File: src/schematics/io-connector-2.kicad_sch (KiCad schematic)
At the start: 1 part

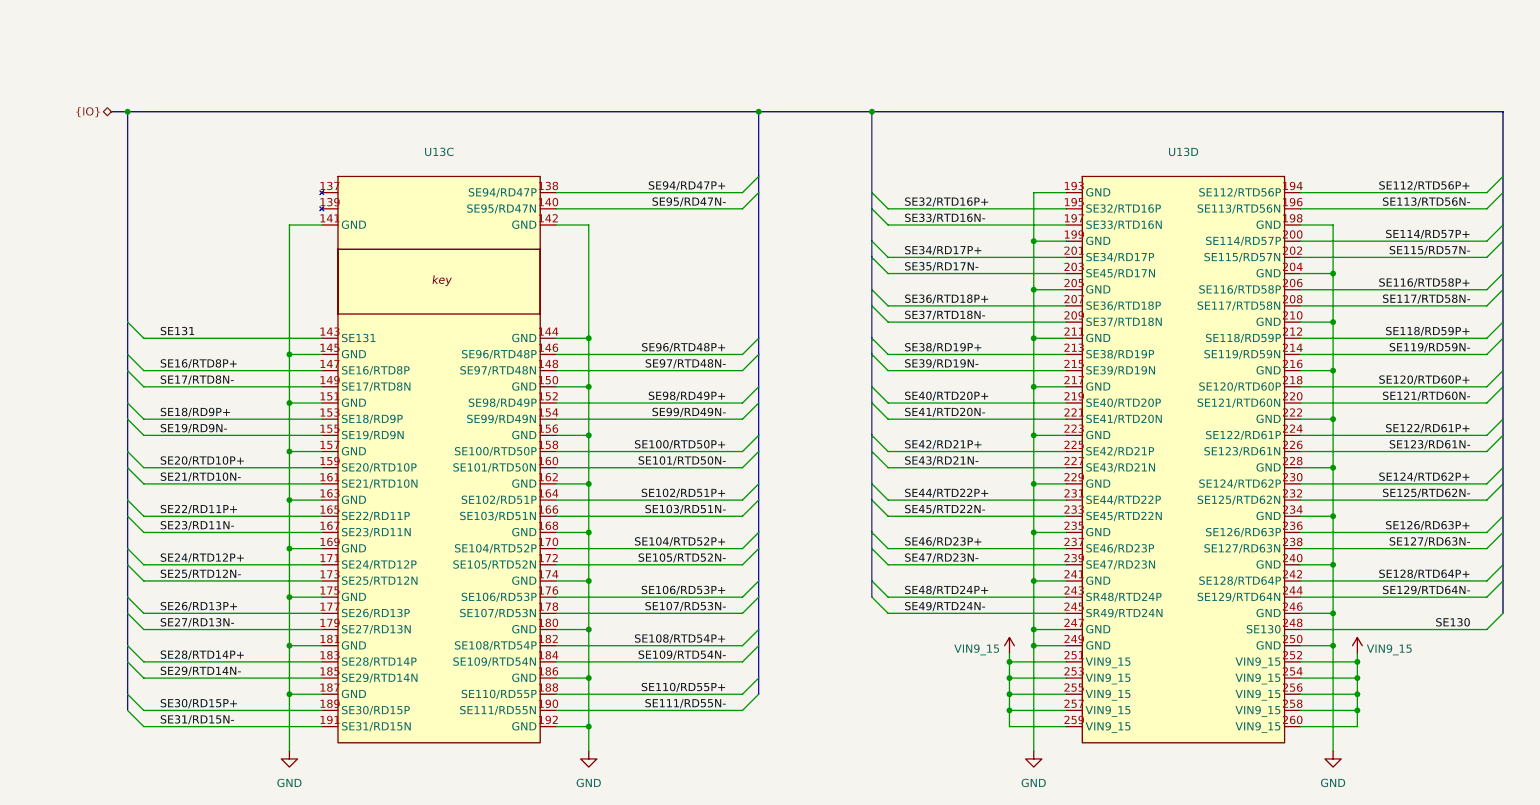
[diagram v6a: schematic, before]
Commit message: ✨ Add net classes to the schematic (#38)
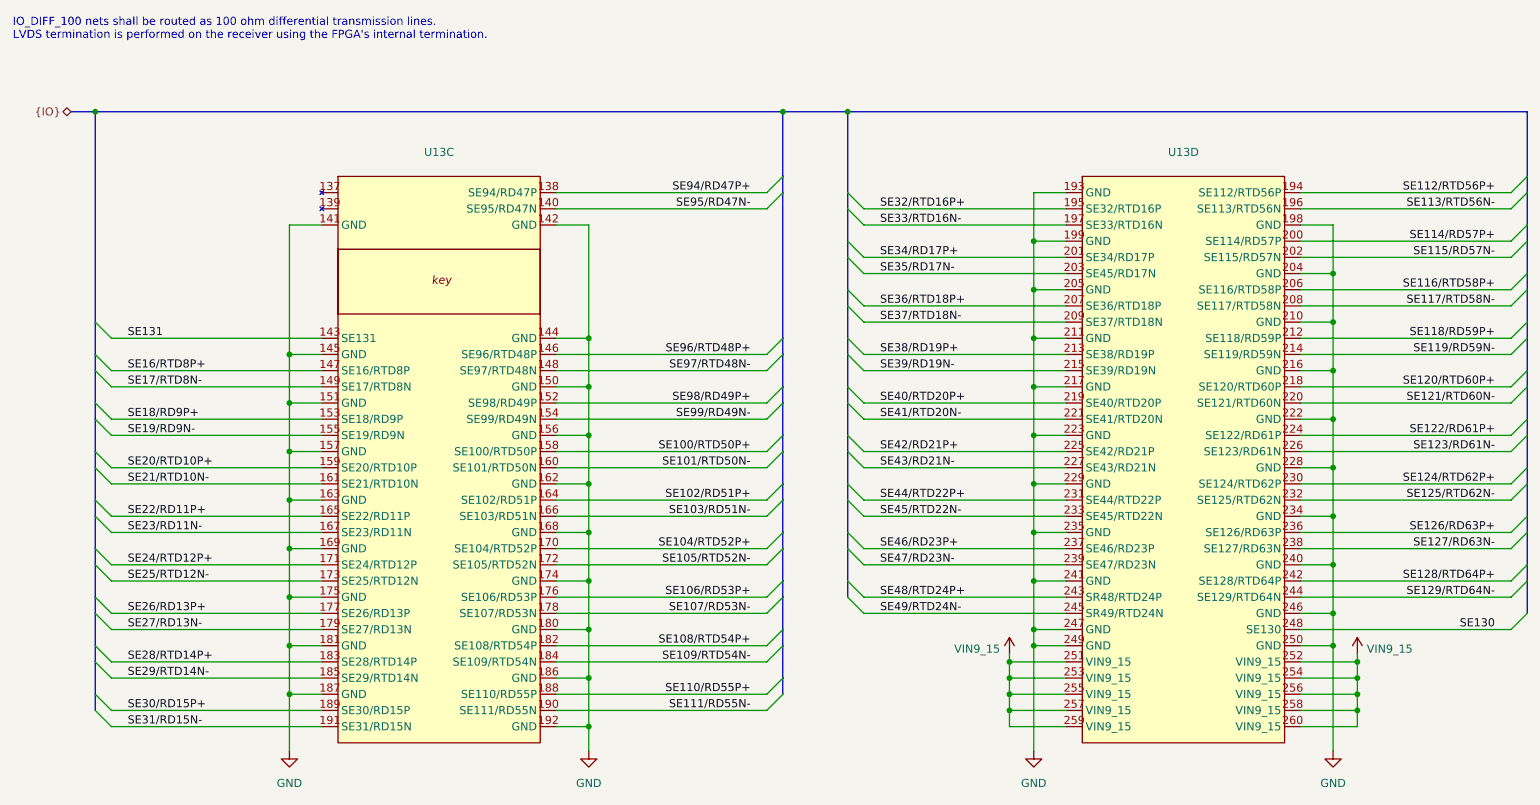
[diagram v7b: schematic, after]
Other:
- note added: "IO_DIFF_100 nets shall be routed as 100 ohm differential transmission lines. LVDS termination is performed on the receiver using the FPGA's internal termination."
